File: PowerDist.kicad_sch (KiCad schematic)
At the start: 15 parts, among them U1 TPS2121RUXR

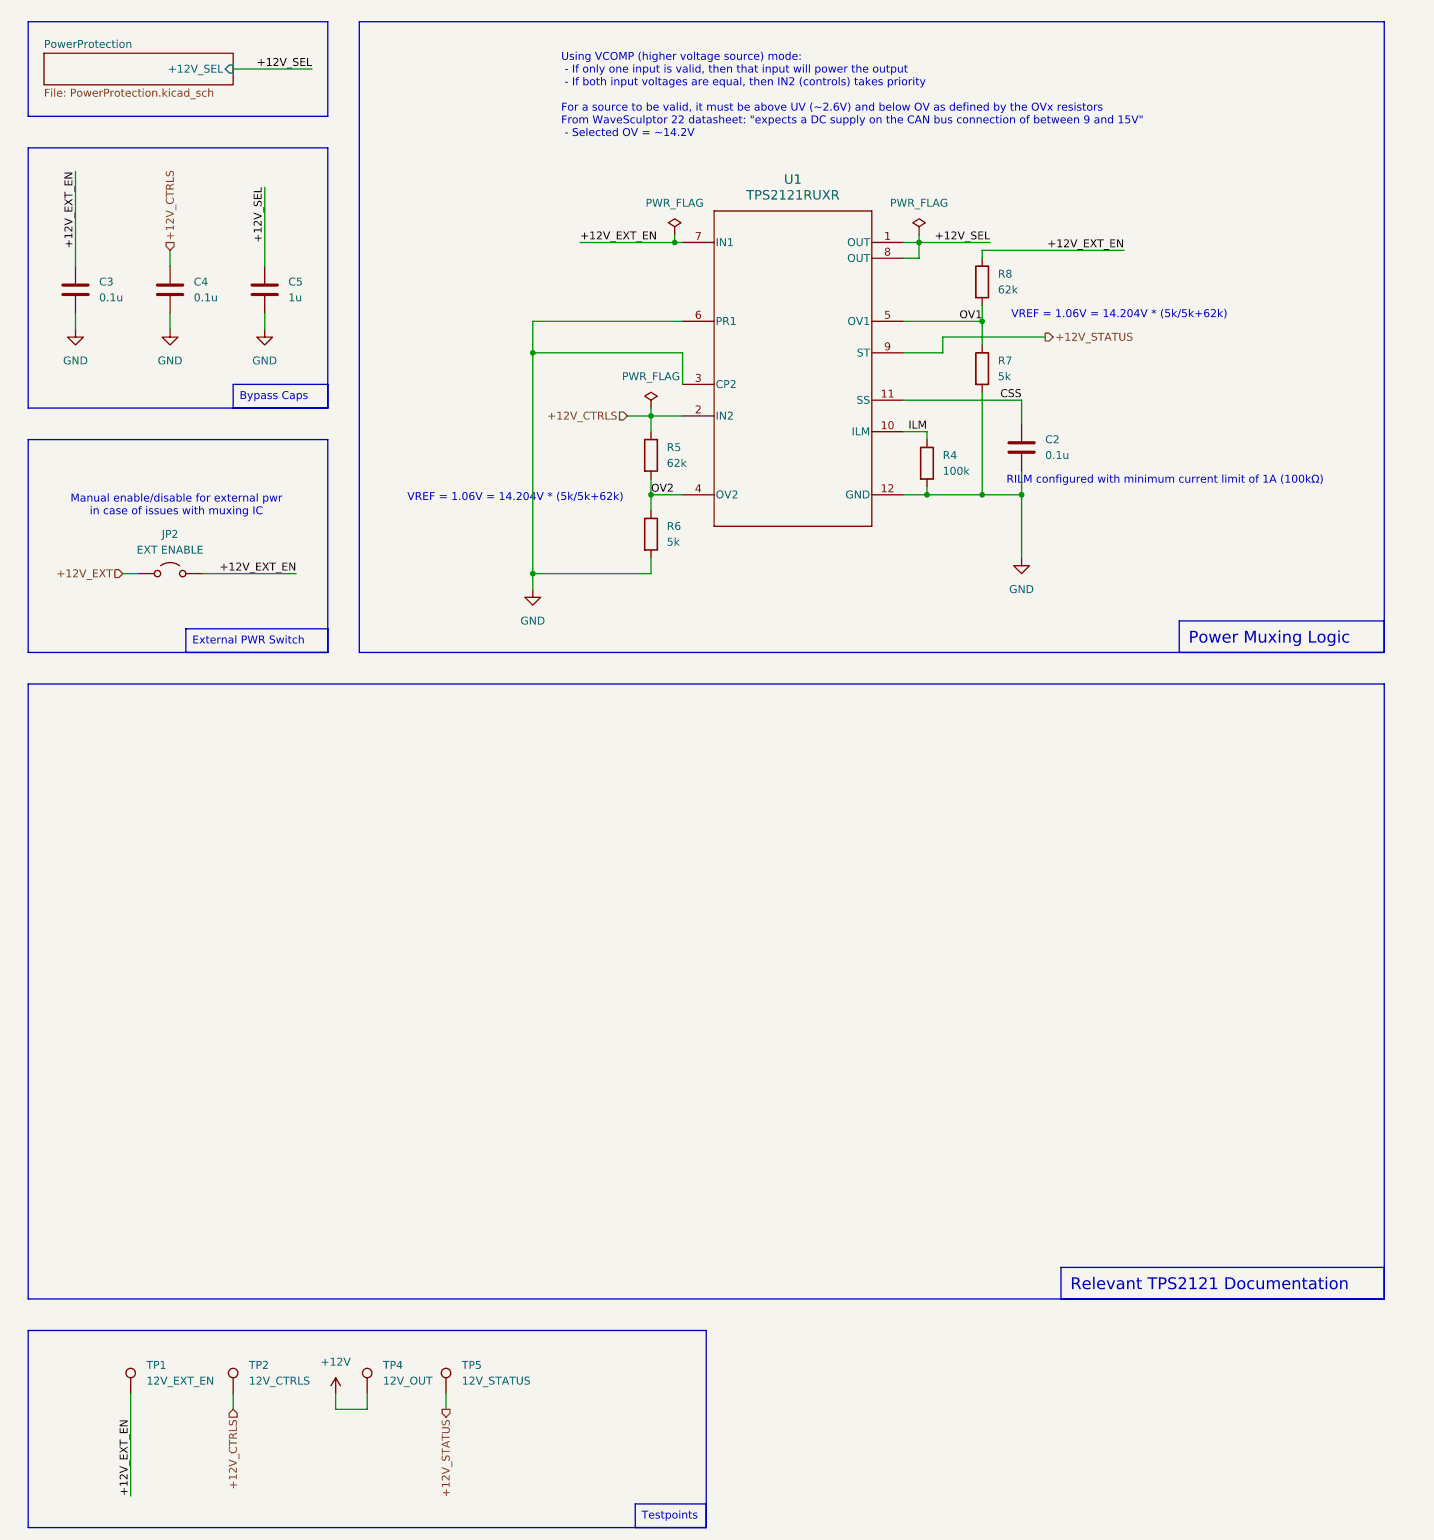
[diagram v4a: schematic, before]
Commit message: add reverse polarity for both inputs, fixed muxing logic i think
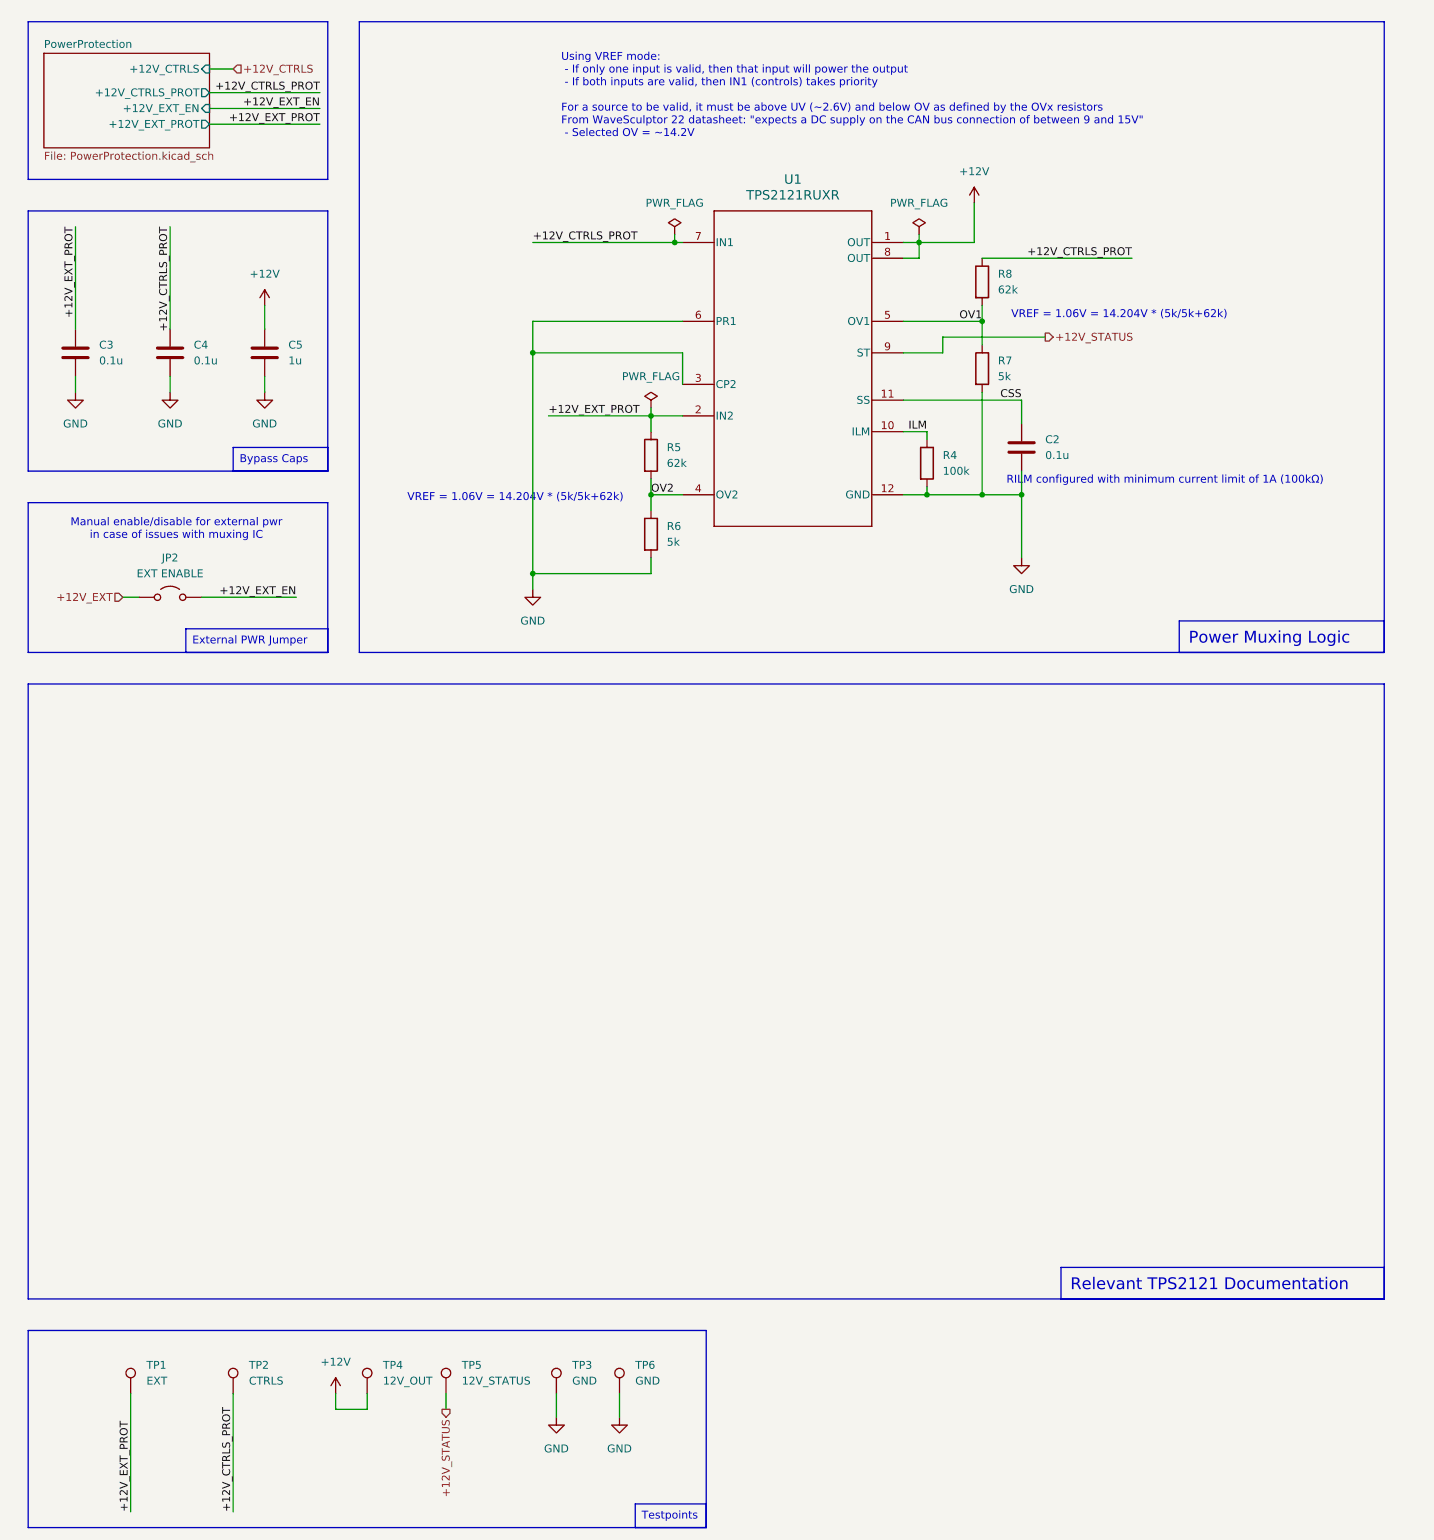
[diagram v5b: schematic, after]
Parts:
- added TP3, TP6: GND, TestPoint:TestPoint_Pad_1.0x1.0mm, symbol Connector:TestPoint
- TP1: value 12V_EXT_EN -> EXT
- TP2: value 12V_CTRLS -> CTRLS
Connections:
- net +12V_SEL is gone; now on net +12V: C5.1, U1.1 (OUT), U1.8 (OUT)
- net +12V_CTRLS: no longer C4.1, R5.1, TP2.1, U1.2 (IN2)
- net +12V_EXT_EN: no longer C3.1, R8.1, TP1.1, U1.7 (IN1)
- net GND: now also TP3.1, TP6.1
- new net +12V_CTRLS_PROT: C4.1, R8.1, TP2.1, U1.7 (IN1)
- new net +12V_EXT_PROT: C3.1, R5.1, TP1.1, U1.2 (IN2)
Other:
- sheet PowerProtection ports: added +12V_CTRLS, +12V_CTRLS_PROT, +12V_EXT_EN, +12V_EXT_PROT; removed +12V_SEL
- note added: "Using VREF mode: - If only one input is valid, then that input will power the output - If both inputs are valid, then IN1 (controls) takes priority For a source to be valid, it must be above UV (~2.6V) and below OV as defined by the OVx resistors From WaveSculptor 22 datasheet: "expects a DC supply on the CAN bus connection of between 9 and 15V" - Selected OV = ~14.2V"
- note removed: "Using VCOMP (higher voltage source) mode: - If only one input is valid, then that input will power the output - If both input voltages are equal, then IN2 (controls) takes priority For a source to be valid, it must be above UV (~2.6V) and below OV as defined by the OVx resistors From WaveSculptor 22 datasheet: "expects a DC supply on the CAN bus connection of between 9 and 15V" - Selected OV = ~1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"
- moved on the sheet: C3, C4, C5, JP2

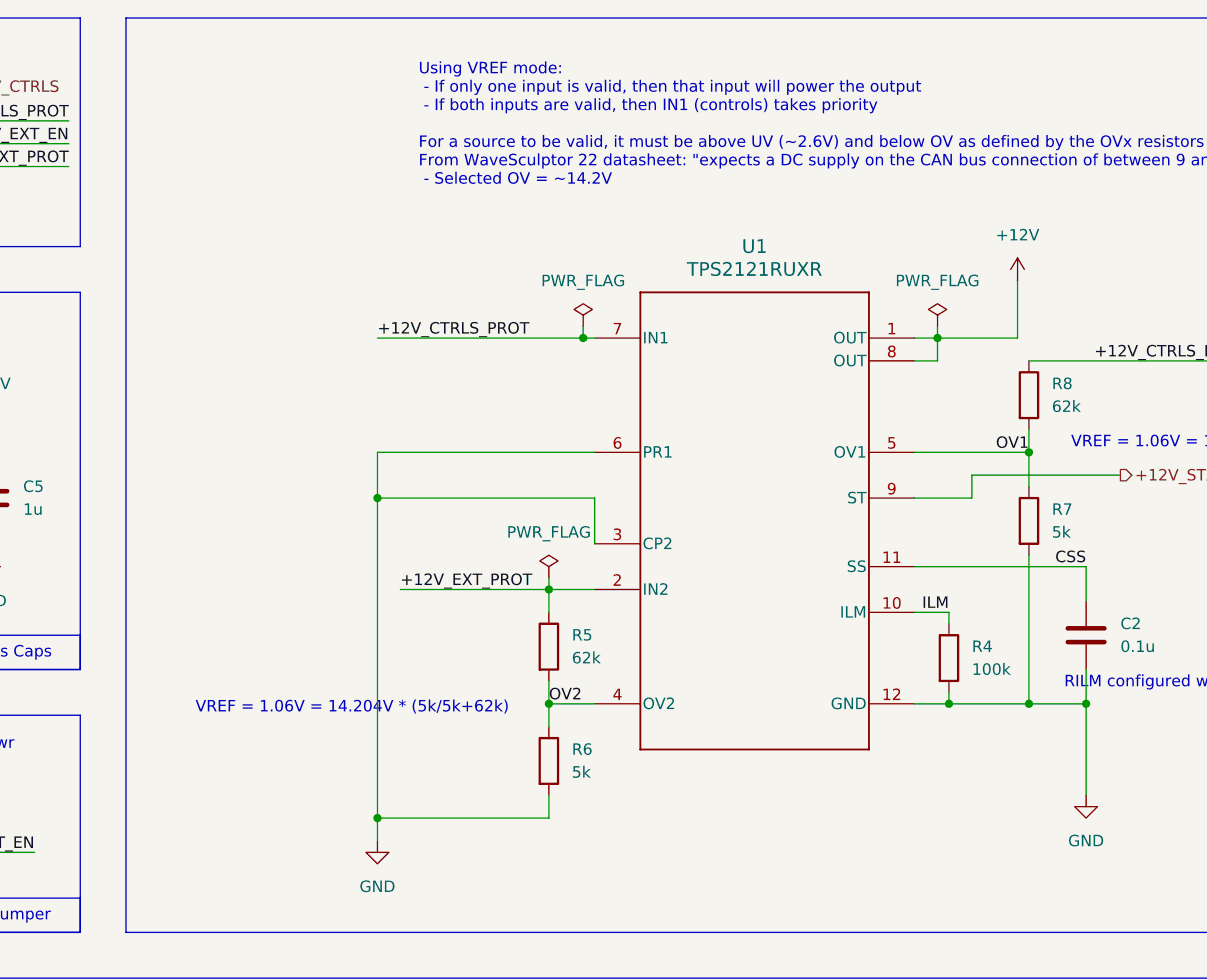
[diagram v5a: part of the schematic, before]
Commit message: proper PR1 pullup
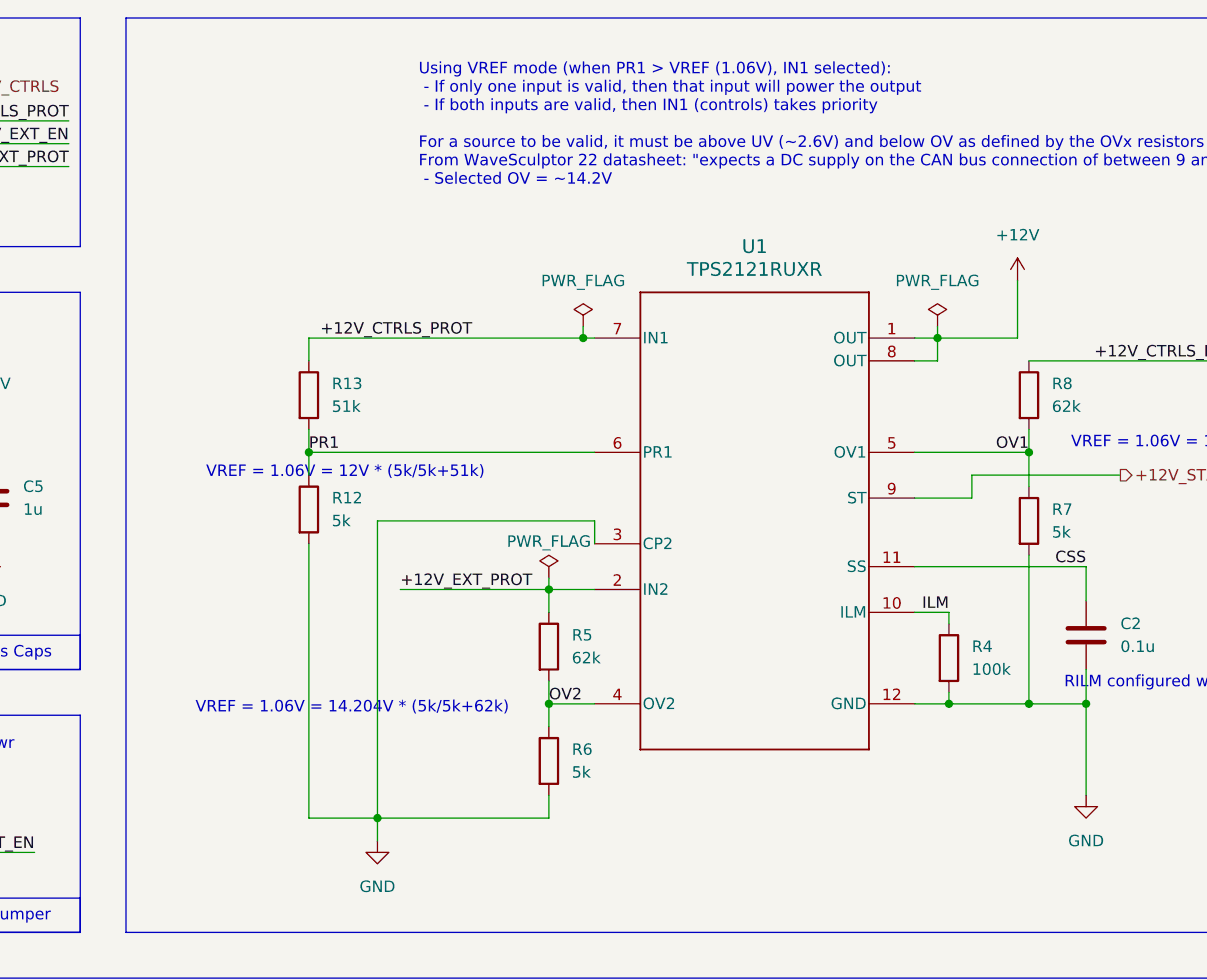
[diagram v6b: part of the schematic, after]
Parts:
- added R12: 5k, Resistor_SMD:R_0805_2012Metric, symbol Device:R
- added R13: 51k, Resistor_SMD:R_0805_2012Metric, symbol Device:R
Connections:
- net +12V_CTRLS_PROT: now also R13.1
- net GND: now also R12.2; no longer U1.6 (PR1)
- new net PR1: R12.1, R13.2, U1.6 (PR1)
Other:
- note added: "Using VREF mode (when PR1 > VREF (1.06V), IN1 selected): - If only one input is valid, then that input will power the output - If both inputs are valid, then IN1 (controls) takes priority For a source to be valid, it must be above UV (~2.6V) and below OV as defined by the OVx resistors From WaveSculptor 22 datasheet: "expects a DC supply on the CAN bus connection of between 9 and 15V" - Selected 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"
- note added: "VREF = 1.06V = 12V * (5k/5k+51k)"
- note removed: "Using VREF mode: - If only one input is valid, then that input will power the output - If both inputs are valid, then IN1 (controls) takes priority For a source to be valid, it must be above UV (~2.6V) and below OV as defined by the OVx resistors From WaveSculptor 22 datasheet: "expects a DC supply on the CAN bus connection of between 9 and 15V" - Selected OV = ~14.2V"
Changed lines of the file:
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@@
 	)
 	(junction
-		(at 100.33 72.39)
+		(at 172.72 67.31)
 		(diameter 0)
 		(color 0 0 0 0)
 	)
 	(junction
-		(at 172.72 67.31)
+		(at 172.72 95.25)
 		(diameter 0)
 		(color 0 0 0 0)
 	)
 	(junction
-		(at 172.72 95.25)
+		(at 92.71 67.31)
 		(diameter 0)
 		(color 0 0 0 0)
@@
 	(wire
 		(pts
-			(xy 100.33 67.31) (xy 100.33 72.39)
+			(xy 86.36 240.03) (xy 86.36 242.57)
 		)
 		(stroke
@@
 	(wire
 		(pts
-			(xy 86.36 240.03) (xy 86.36 242.57)
+			(xy 172.72 78.74) (xy 172.72 95.25)
 		)
 		(stroke
@@
 	(wire
 		(pts
-			(xy 172.72 78.74) (xy 172.72 95.25)
+			(xy 48.26 26.67) (xy 52.07 26.67)
 		)
 		(stroke
@@
 	(wire
 		(pts
-			(xy 48.26 26.67) (xy 52.07 26.67)
+			(xy 57.15 64.77) (xy 57.15 68.58)
 		)
 		(stroke
@@
 	(wire
 		(pts
-			(xy 57.15 64.77) (xy 57.15 68.58)
+			(xy 92.71 54.61) (xy 123.19 54.61)
 		)
 		(stroke
@@
 	(wire
 		(pts
-			(xy 124.46 72.39) (xy 124.46 77.47)
+			(xy 124.46 74.93) (xy 124.46 77.47)
 		)
 		(stroke
@@
 	(wire
 		(pts
-			(xy 100.33 54.61) (xy 123.19 54.61)
+			(xy 92.71 77.47) (xy 92.71 107.95)
 		)
 		(stroke
@@
 	(wire
 		(pts
-			(xy 124.46 67.31) (xy 100.33 67.31)
+			(xy 166.37 69.85) (xy 166.37 72.39)
 		)
 		(stroke
@@
 	(wire
 		(pts
-			(xy 166.37 69.85) (xy 166.37 72.39)
+			(xy 26.67 52.07) (xy 26.67 68.58)
 		)
 		(stroke
@@
 	(wire
 		(pts
-			(xy 26.67 52.07) (xy 26.67 68.58)
+			(xy 92.71 54.61) (xy 92.71 57.15)
 		)
 		(stroke
@@
 	(wire
 		(pts
-			(xy 100.33 72.39) (xy 124.46 72.39)
+			(xy 100.33 74.93) (xy 124.46 74.93)
 		)
 		(stroke
@@
 	(wire
 		(pts
+			(xy 92.71 64.77) (xy 92.71 67.31)
+		)
+		(stroke
+			(width 0)
+			(type default)
+		)
+	)
+	(wire
+		(pts
 			(xy 172.72 64.77) (xy 172.72 67.31)
 		)
@@
 	(wire
 		(pts
+			(xy 92.71 107.95) (xy 100.33 107.95)
+		)
+		(stroke
+			(width 0)
+			(type default)
+		)
+	)
+	(wire
+		(pts
 			(xy 172.72 57.15) (xy 196.85 57.15)
 		)
@@
 	(wire
 		(pts
-			(xy 100.33 72.39) (xy 100.33 107.95)
+			(xy 100.33 74.93) (xy 100.33 107.95)
 		)
 		(stroke
@@
 	(wire
 		(pts
+			(xy 92.71 69.85) (xy 92.71 67.31)
+		)
+		(stroke
+			(width 0)
+			(type default)
+		)
+	)
+	(wire
+		(pts
 			(xy 123.19 53.34) (xy 123.19 54.61)
 		)
@@
 		)
 	)
+	(wire
+		(pts
+			(xy 92.71 67.31) (xy 124.46 67.31)
+		)
+		(stroke
+			(width 0)
+			(type default)
+		)
+	)
 	(rectangle
 		(start 19.05 229.87)
@@
 		)
 	)
-	(text "Using VREF mode:\n - If only one input is valid, then that input will power the output\n - If both inputs are valid, then IN1 (controls) takes priority\n\nFor a source to be valid, it must be above UV (~2.6V) and below OV as defined by the OVx resistors\nFrom WaveSculptor 22 datasheet: \"expects a DC supply on the CAN bus connection of between 9 and 15V\"\n - Selected OV = ~14.2V"
+	(text "VREF = 1.06V = 12V * (5k/5k+51k)"
+		(exclude_from_sim no)
+		(at 96.774 69.596 0)
+		(effects
+			(font
+				(size 1.27 1.27)
+			)
+		)
+	)
+	(text "Using VREF mode (when PR1 > VREF (1.06V), IN1 selected):\n - If only one input is valid, then that input will power the output\n - If both inputs are valid, then IN1 (controls) takes priority\n\nFor a source to be valid, it must be above UV (~2.6V) and below OV as defined by the OVx resistors\nFrom WaveSculptor 22 datasheet: \"expects a DC supply on the CAN bus connection of between 9 and 15V\"\n - Selected OV = ~14.2V"
 		(exclude_from_sim no)
 		(at 104.902 30.988 0)
@@
 		)
 	)
+	(label "PR1"
+		(at 92.71 67.31 0)
+		(fields_autoplaced yes)
+		(effects
+			(font
+				(size 1.27 1.27)
+			)
+			(justify left bottom)
+		)
+	)
 	(label "+12V_EXT_PROT"
 		(at 26.67 52.07 270)
@@
 	)
 	(label "+12V_CTRLS_PROT"
-		(at 100.33 54.61 0)
+		(at 93.98 54.61 0)
 		(fields_autoplaced yes)
 		(effects
@@
 	)
 	(symbol
+		(lib_id "Device:R")
+		(at 92.71 60.96 0)
+		(unit 1)
+		(exclude_from_sim no)
+		(in_bom yes)
+		(on_board yes)
+		(dnp no)
+		(fields_autoplaced yes)
+		(property "Reference" "R13"
+			(at 95.25 59.6899 0)
+			(effects
+				(font
+					(size 1.27 1.27)
+				)
+				(justify left)
+			)
+		)
+		(property "Value" "51k"
+			(at 95.25 62.2299 0)
+			(effects
+				(font
+					(size 1.27 1.27)
+				)
+				(justify left)
+			)
+		)
+		(property "Footprint" "Resistor_SMD:R_0805_2012Metric"
+			(at 90.932 60.96 90)
+			(effects
+				(font
+					(size 1.27 1.27)
+				)
+				(hide yes)
+			)
+		)
+		(property "Datasheet" "~"
+			(at 92.71 60.96 0)
+			(effects
+				(font
+					(size 1.27 1.27)
+				)
+				(hide yes)
+			)
+		)
+		(property "Description" "Resistor"
+			(at 92.71 60.96 0)
+			(effects
+				(font
+					(size 1.27 1.27)
+				)
+				(hide yes)
+			)
+		)
+		(pin "2"
+		)
+		(pin "1"
+		)
+		(instances
+			(project "Controls-MotorControllerBreakout"
+				(path "/0a971d65-5373-49c6-bc07-3a5d4263dbef/2da5a7b5-cad0-4d65-bb48-cd65e4f2745e"
+					(reference "R13")
+					(unit 1)
+				)
+			)
+		)
+	)
+	(symbol
 		(lib_id "power:GND")
 		(at 179.07 105.41 0)
@@
 		(on_board yes)
 		(dnp no)
-		(fields_autoplaced yes)
 		(property "Reference" "#FLG02"
 			(at 119.38 79.375 0)
@@
 		)
 		(property "Value" "PWR_FLAG"
-			(at 119.38 76.2 0)
+			(at 119.38 77.216 0)
 			(effects
 				(font
@@
 					(unit 1)
 				)
+			)
+		)
+	)
+	(symbol
+		(lib_id "Device:R")
+		(at 92.71 73.66 0)
+		(unit 1)
+		(exclude_from_sim no)
+		(in_bom yes)
+		(on_board yes)
+		(dnp no)
+		(fields_autoplaced yes)
+		(property "Reference" "R12"
+			(at 95.25 72.3899 0)
+			(effects
+				(font
+					(size 1.27 1.27)
+				)
+				(justify left)
+			)
+		)
+		(property "Value" "5k"
+			(at 95.25 74.9299 0)
+			(effects
+				(font
+					(size 1.27 1.27)
+				)
+				(justify left)
+			)
+		)
+		(property "Footprint" "Resistor_SMD:R_0805_2012Metric"
+			(at 90.932 73.66 90)
+			(effects
+				(font
+					(size 1.27 1.27)
+				)
+				(hide yes)
+			)
+		)
+		(property "Datasheet" "~"
+			(at 92.71 73.66 0)
+			(effects
+				(font
+					(size 1.27 1.27)
+				)
+				(hide yes)
+			)
+		)
+		(property "Description" "Resistor"
+			(at 92.71 73.66 0)
+			(effects
+				(font
+					(size 1.27 1.27)
+				)
+				(hide yes)
+			)
+		)
+		(pin "2"
+		)
+		(pin "1"
+		)
+		(instances
+			(project "Controls-MotorControllerBreakout"
+				(path "/0a971d65-5373-49c6-bc07-3a5d4263dbef/2da5a7b5-cad0-4d65-bb48-cd65e4f2745e"
+					(reference "R12")
+					(unit 1)
+				)
